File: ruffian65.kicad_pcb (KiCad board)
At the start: 2 copper layers, 304.8 x 95.3 mm, 7 parts, among them SW22 Y, SW23 U, SW4 #3, SW42 ', SW58 UP, SW8 #7, SW9 #8

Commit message: wiring done?
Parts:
- added SW62: LALT, MX_Only:MXOnly-1.5U-Hotswap, F.Cu at (57.1, 139.7)
- added SW66: FN, MX_Only:MXOnly-1.5U-Hotswap, F.Cu at (219.1, 139.7)
- added U1: ATmega32U4-MU, Package_DFN_QFN:QFN-44-1EP_7x7mm_P0.5mm_EP5.2x5.2mm, B.Cu at (203.2, 137.3)
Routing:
- net row2: track 0.00 -> 523.2 mm, vias 0 -> 4
- net col0: track 0.00 -> 478.9 mm, vias 0 -> 7
- net GND: track 0.00 -> 435.7 mm, vias 0 -> 8
- net row0: track 0.00 -> 418.1 mm, vias 0 -> 4
- net col3: track 0.00 -> 365.4 mm, vias 0 -> 5
- net +5V: track 0.00 -> 354.2 mm, vias 0 -> 9
- net row3: track 0.00 -> 349.9 mm, vias 0 -> 8
- net row1: track 0.00 -> 332.9 mm, vias 0 -> 6
- net row4: track 0.00 -> 295.1 mm, vias 0 -> 2
- net col1: track 0.00 -> 288.8 mm, vias 0 -> 5
- net col2: track 0.00 -> 252.6 mm, vias 0 -> 5
- net col14: track 0.00 -> 206.5 mm, vias 0 -> 7
- net col4: track 0.00 -> 200.7 mm, vias 0 -> 13
- net col12: track 0.00 -> 190.8 mm, vias 0 -> 8
- net col13: track 0.00 -> 187.4 mm, vias 0 -> 6
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- added copper zone on B.Cu, net GND
- added copper zone on F.Cu, net GND

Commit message: wiring finished
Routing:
- net row2: track 523.2 -> 521.1 mm
- net col12: track 190.8 -> 192.1 mm
- net MOSI: track 33.5 -> 32.7 mm

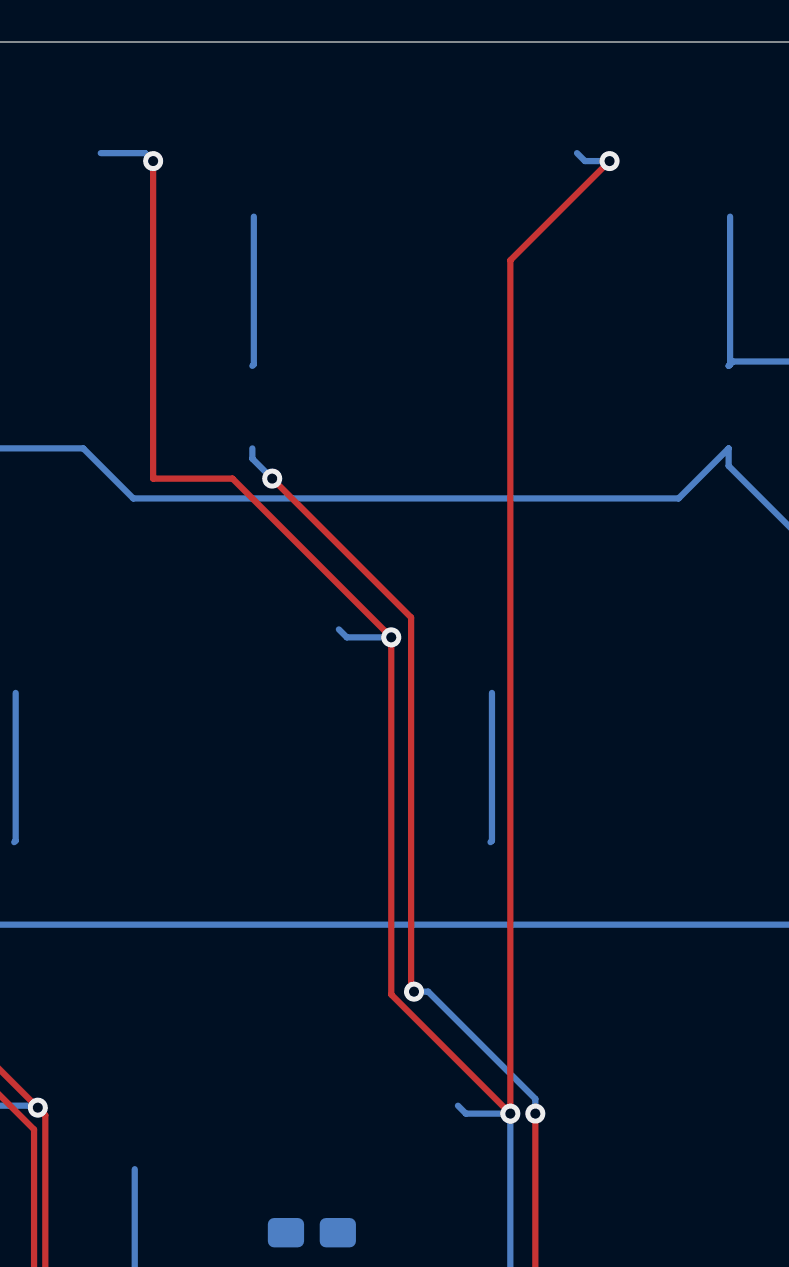
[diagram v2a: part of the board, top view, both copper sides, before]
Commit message: small track fix
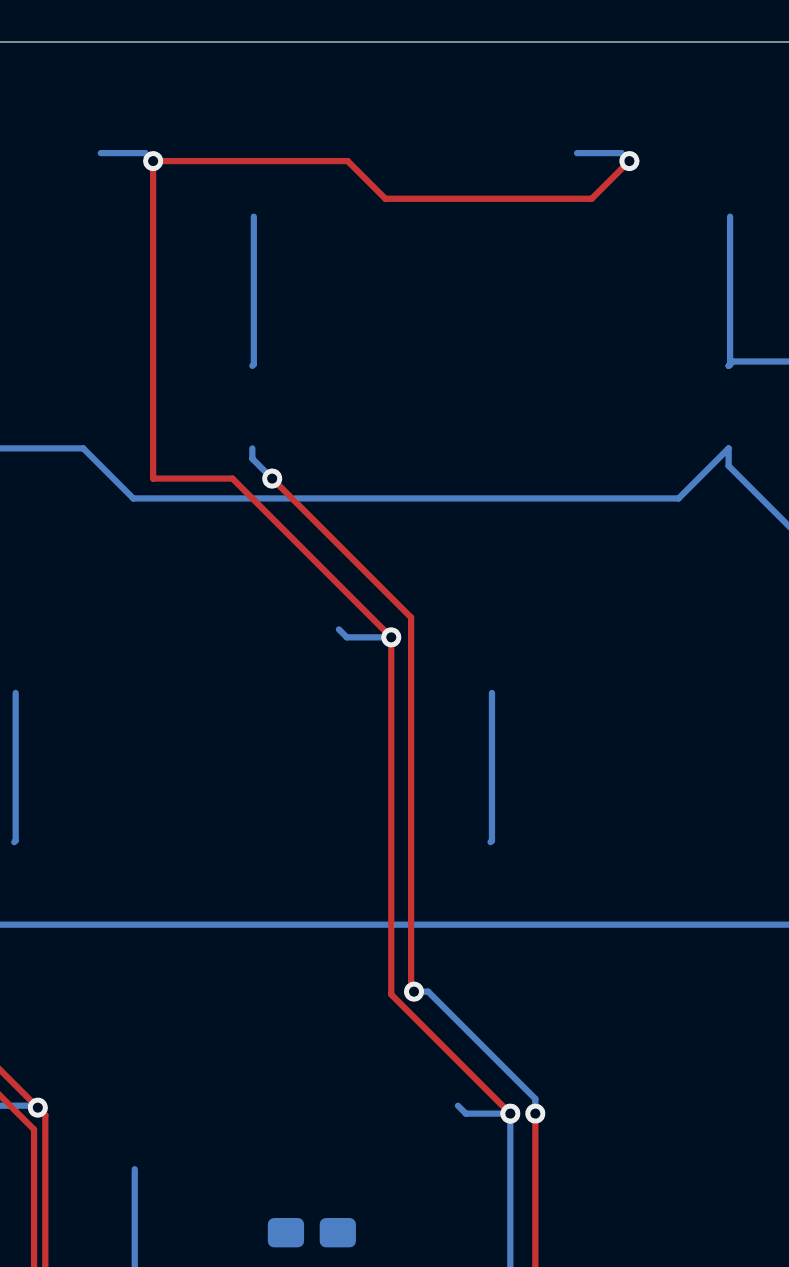
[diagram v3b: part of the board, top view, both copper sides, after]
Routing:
- net col11: track 162.8 -> 144.1 mm

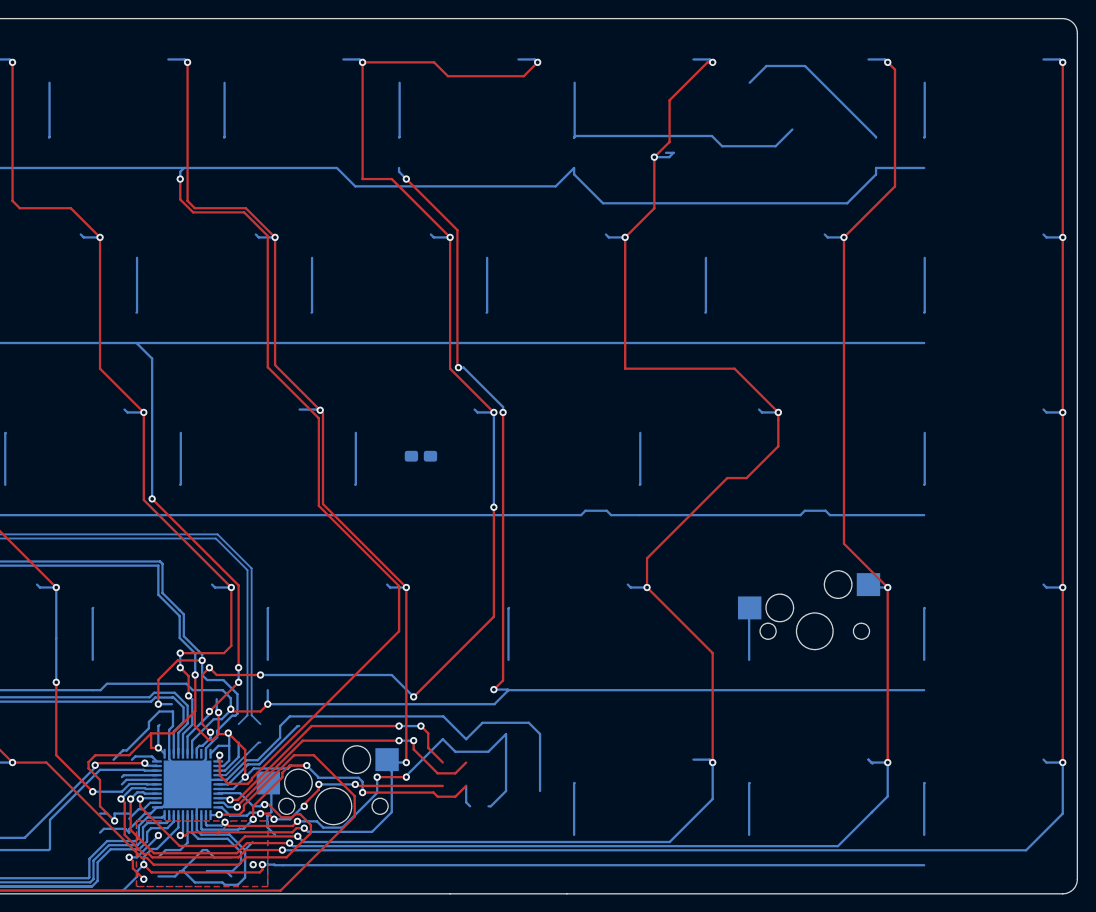
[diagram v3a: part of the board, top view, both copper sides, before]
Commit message: added ec11
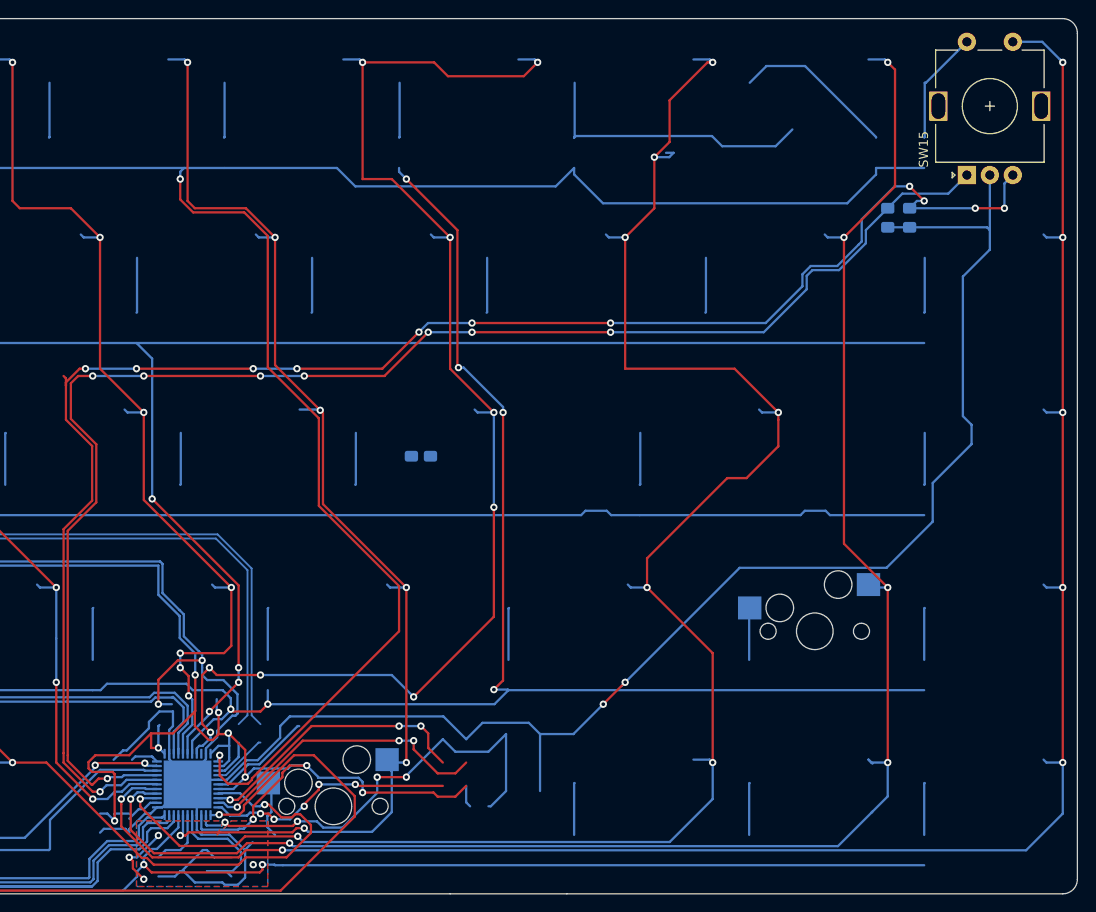
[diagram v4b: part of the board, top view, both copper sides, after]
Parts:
- added C10: 100nF, Capacitor_SMD:C_0805_2012Metric_Pad1.18x1.45mm_HandSolder, B.Cu at (279.4, 75.7)
- added C9: 100nF, Capacitor_SMD:C_0805_2012Metric_Pad1.18x1.45mm_HandSolder, B.Cu at (281.8, 75.7)
- added SW15: Rotary_Encoder_Switch, Keebio-Parts:RotaryEncoder_Alps_EC11E-Switch_Vertical_H20mm, F.Cu at (290.5, 63.5)
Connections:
- U1 pad 29: Net-(U1-Pad29) -> rot0
- U1 pad 30: Net-(U1-Pad30) -> rot1
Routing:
- net rot0: track 0.00 -> 178.3 mm, vias 0 -> 12
- net rot1: track 0.00 -> 163.3 mm, vias 0 -> 8
- net GND: track 435.6 -> 540.8 mm, vias 8 -> 10
- net Net-(D15-Pad2): track 5.99 -> 12.4 mm
- net col14: track 206.5 -> 210.7 mm
- net Net-(U1-Pad29): track 4.01 -> 0.00 mm
- net Net-(U1-Pad30): track 3.89 -> 0.00 mm
- net +5V: track 354.2 -> 355.5 mm
- net col8: track 110.4 -> 111.5 mm

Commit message: encoder support?
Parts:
- added J2: USB_C_Receptacle_USB2.0, Connector_USB:USB_C_Receptacle_HRO_TYPE-C-31-M-12, B.Cu at (13.9, 56.3)
- added SW2: #1, MX_Only:MXOnly-1U-Hotswap, F.Cu at (23.8, 63.5)
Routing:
- net Net-(J2-PadA5): track 0.00 -> 14.5 mm, vias 0 -> 2
- net Net-(R6-Pad1): track 14.0 -> 0.00 mm, vias 2 -> 0
- net Net-(J2-PadB5): track 0.00 -> 4.25 mm
- net Net-(R5-Pad1): track 3.71 -> 0.00 mm
- net rot0: track 178.3 -> 177.2 mm
- net VCC: track 24.8 -> 25.7 mm
